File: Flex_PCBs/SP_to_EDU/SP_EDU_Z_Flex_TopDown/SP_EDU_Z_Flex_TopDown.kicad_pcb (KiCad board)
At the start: 2 copper layers, 4.5 x 64 mm, 2 parts, among them J1 Conn_01x08_Male, J2 Conn_01x08_Male

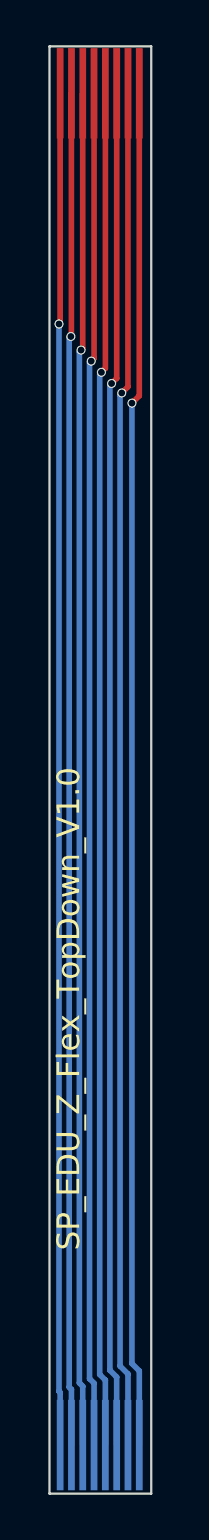
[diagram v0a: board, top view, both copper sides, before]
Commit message: replace ZF5S-*-01-T-WT and 2005280040 connectors with T1M-*-F-SH-L-FR connector
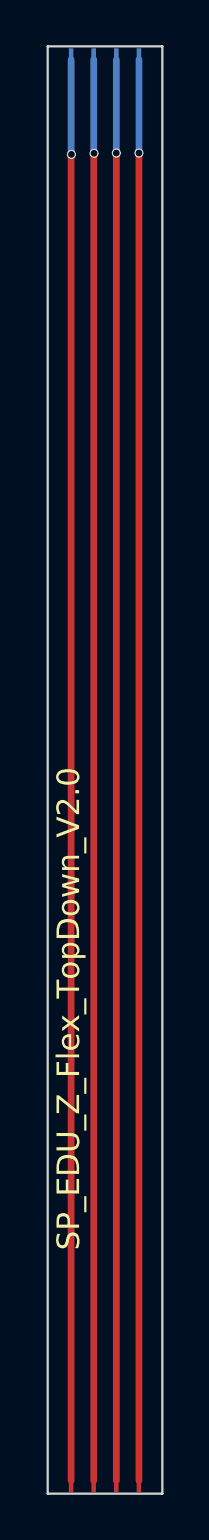
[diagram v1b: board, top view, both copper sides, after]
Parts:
- J1: value Conn_01x08_Male -> Conn_01x04_Pin; footprint STS_connector:flexpcb con. -> STS_connector:flexPCB_connector_edu_sensors_new; moved to B.Cu
- J2: value Conn_01x08_Male -> Conn_01x04_Pin; footprint STS_connector:flexpcb con. -> STS_connector:flexPCB_connector_edu_sensors_new; moved to F.Cu
- moved J1 6.00 mm to (127.5, 44.8), turned to 180 degrees
- moved J2 4.12 mm to (123.5, 107.6), turned to 0 degrees
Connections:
- J1 pad 1: 8 -> 4
- J1 pad 2: 7 -> 3
- J1 pad 3: 6 -> 2
- J1 pad 4: 5 -> 1
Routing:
- net 5: track 60.0 -> 0.00 mm, vias 1 -> 0
- net 6: track 59.9 -> 0.00 mm, vias 1 -> 0
- net 7: track 59.9 -> 0.00 mm, vias 1 -> 0
- net 8: track 59.8 -> 0.00 mm, vias 1 -> 0
- net 4: track 60.0 -> 62.8 mm
- net 3: track 60.0 -> 62.8 mm
- net 1: track 60.0 -> 62.9 mm
- net 2: track 60.1 -> 62.9 mm
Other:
- board size 4.5 x 64 mm -> 5.1 x 64 mm
- board text added: "SP_EDU_Z_Flex_TopDown_V2.0"
- board text removed: "SP_EDU_Z_Flex_TopDown_V1.0"
